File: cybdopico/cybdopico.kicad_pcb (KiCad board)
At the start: 2 copper layers, 21 x 51 mm, 35 parts, among them P1 USB_C_Plug_USB2.0, SW1 BOOTSEL, SW2 RESET, SW3 HC FLAG, U1 RP2040, U2 USBLC6-2SC6, U3 W25Q16JVUXIQ, U4 MCP1700x-330xxTT, Y1 ABM8-272-T3

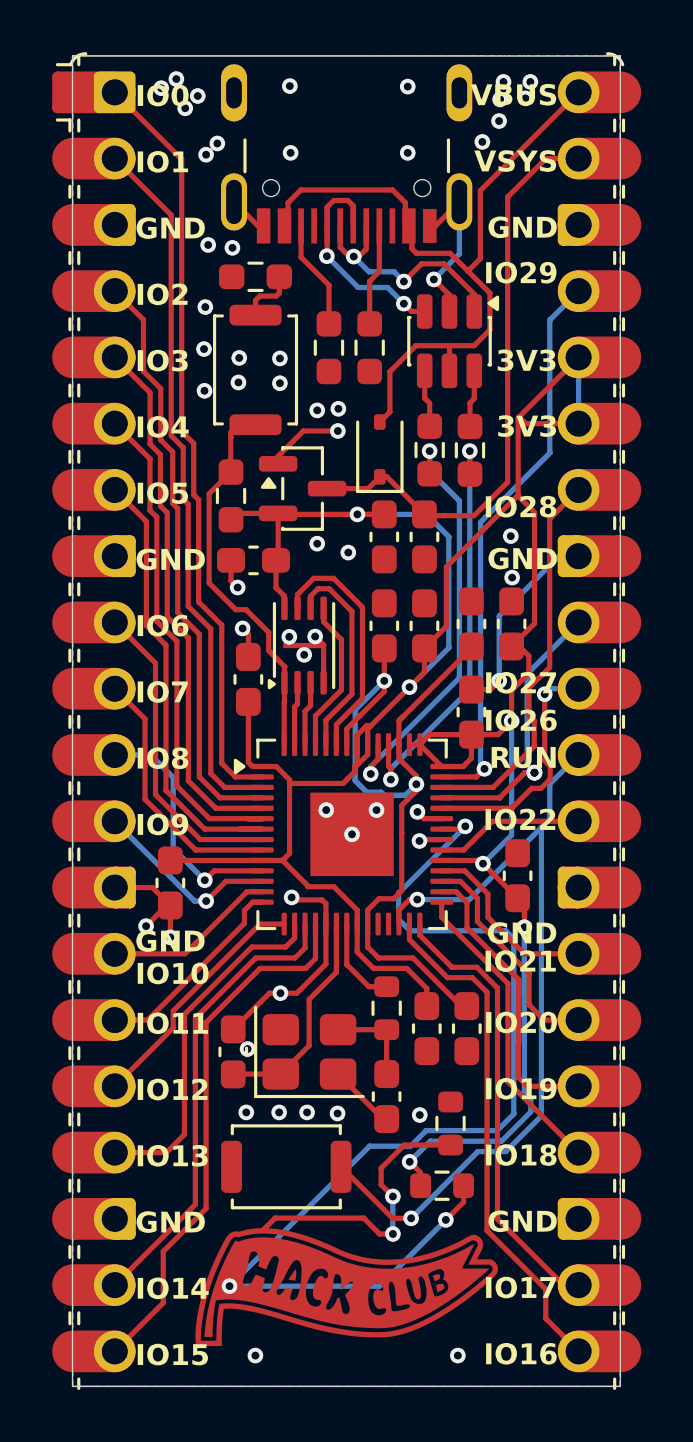
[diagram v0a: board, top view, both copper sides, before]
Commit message: fixed resistors and clearned up board (extra vias, traces, etc)
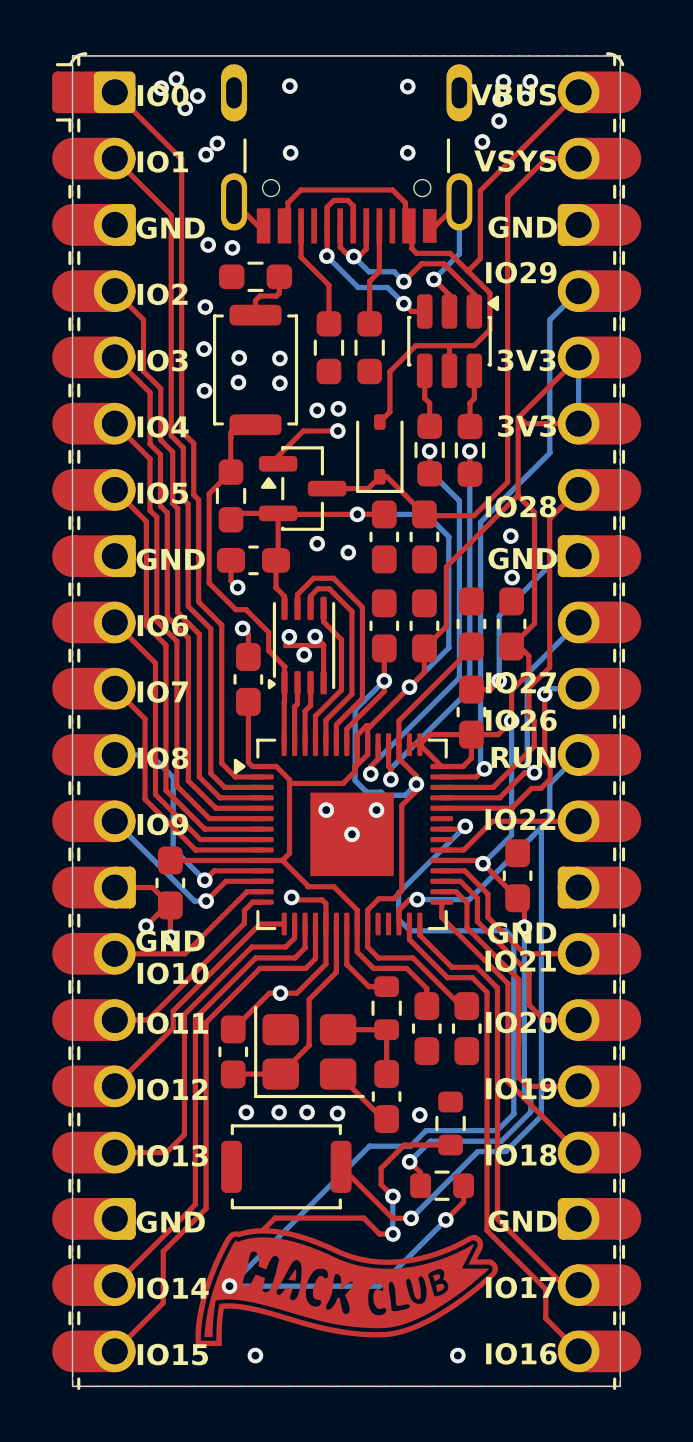
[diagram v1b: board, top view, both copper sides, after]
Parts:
- R3, R4: value 27R -> 5k1R
- R5: value 27R -> 10kR
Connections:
- U1 pad 35: GPIO23-PHYS-BTN -> unconnected-(U1-GPIO23-Pad35)
- U1 pad 37: GPIO25-LED -> unconnected-(U1-GPIO25-Pad37)
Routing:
- net +3V3: track 115.3 -> 110.8 mm
- net GPIO17: track 18.1 -> 16.7 mm
- net GPIO4: track 19.8 -> 18.7 mm
- net FLASH_SS: track 15.2 -> 14.2 mm
- net GPIO25-LED: track 1.04 -> 0.00 mm, vias 1 -> 0
- net GPIO23-PHYS-BTN: track 0.87 -> 0.00 mm, vias 1 -> 0
- net GPIO5: track 17.5 -> 16.6 mm
- net +1V1: track 30.4 -> 29.8 mm
- net GND: track 38.3 -> 38.1 mm, vias 54 -> 53
- net GPIO27: track 10.7 -> 10.6 mm, vias 2 -> 1

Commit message: made production files
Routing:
- net GND: track 38.1 -> 62.2 mm
- net Net-(R8-Pad1): track 11.3 -> 8.54 mm, vias 2 -> 0
- net +3V3: track 110.8 -> 112.0 mm
- net RUN: track 31.8 -> 33.1 mm
